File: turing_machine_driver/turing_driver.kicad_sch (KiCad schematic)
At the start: 28 parts, among them J1 Buttons and Switches connector, Q1 55NF06, U1 74LS14, U2 74LS03, U3 74LS04, U4 74LS139, U5 74LS74, U6 NE555P

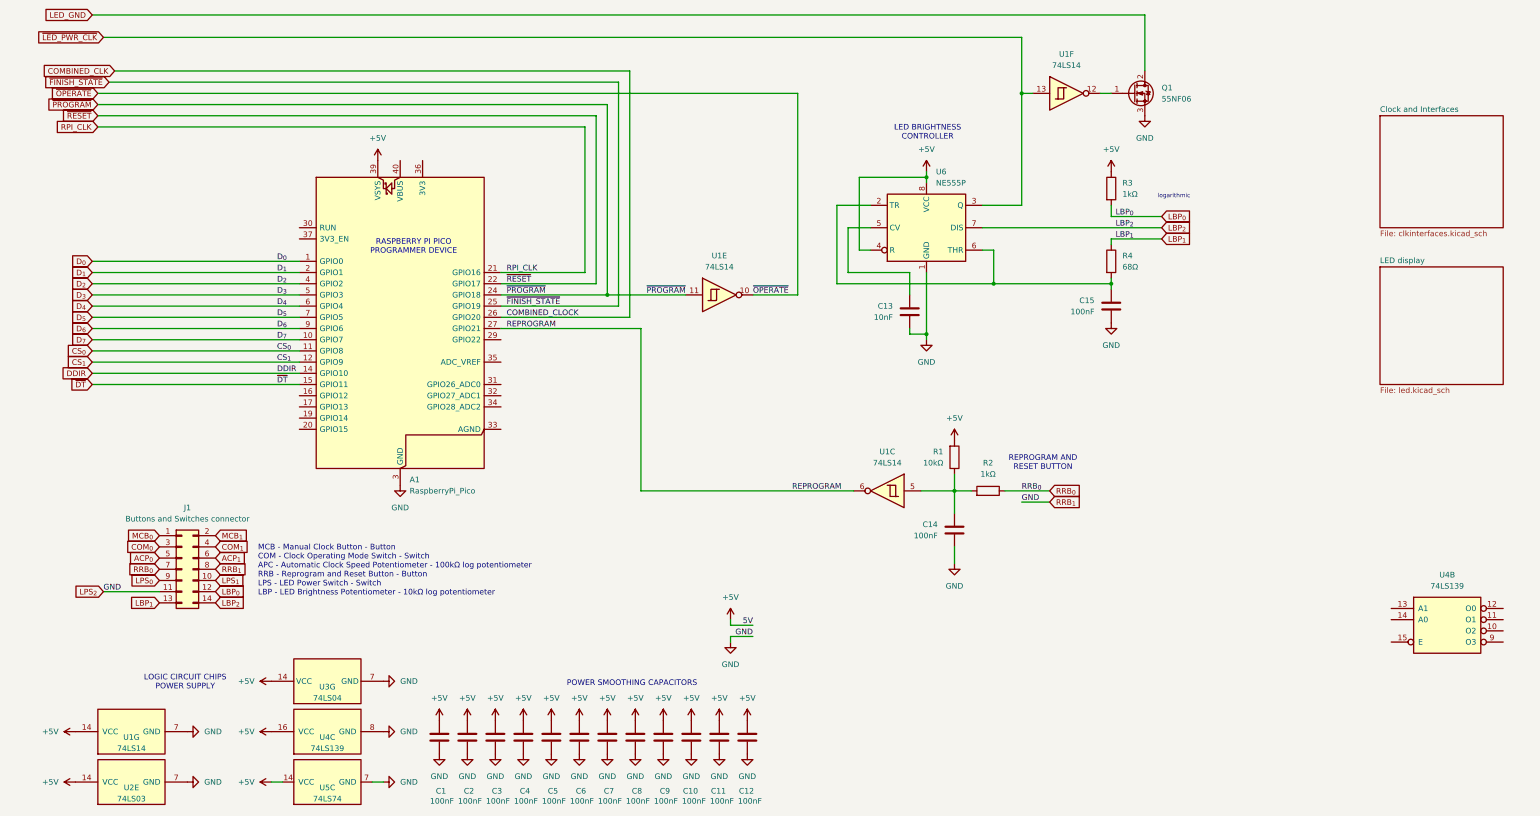
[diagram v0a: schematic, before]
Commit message: added control panel and moved LEDs to it
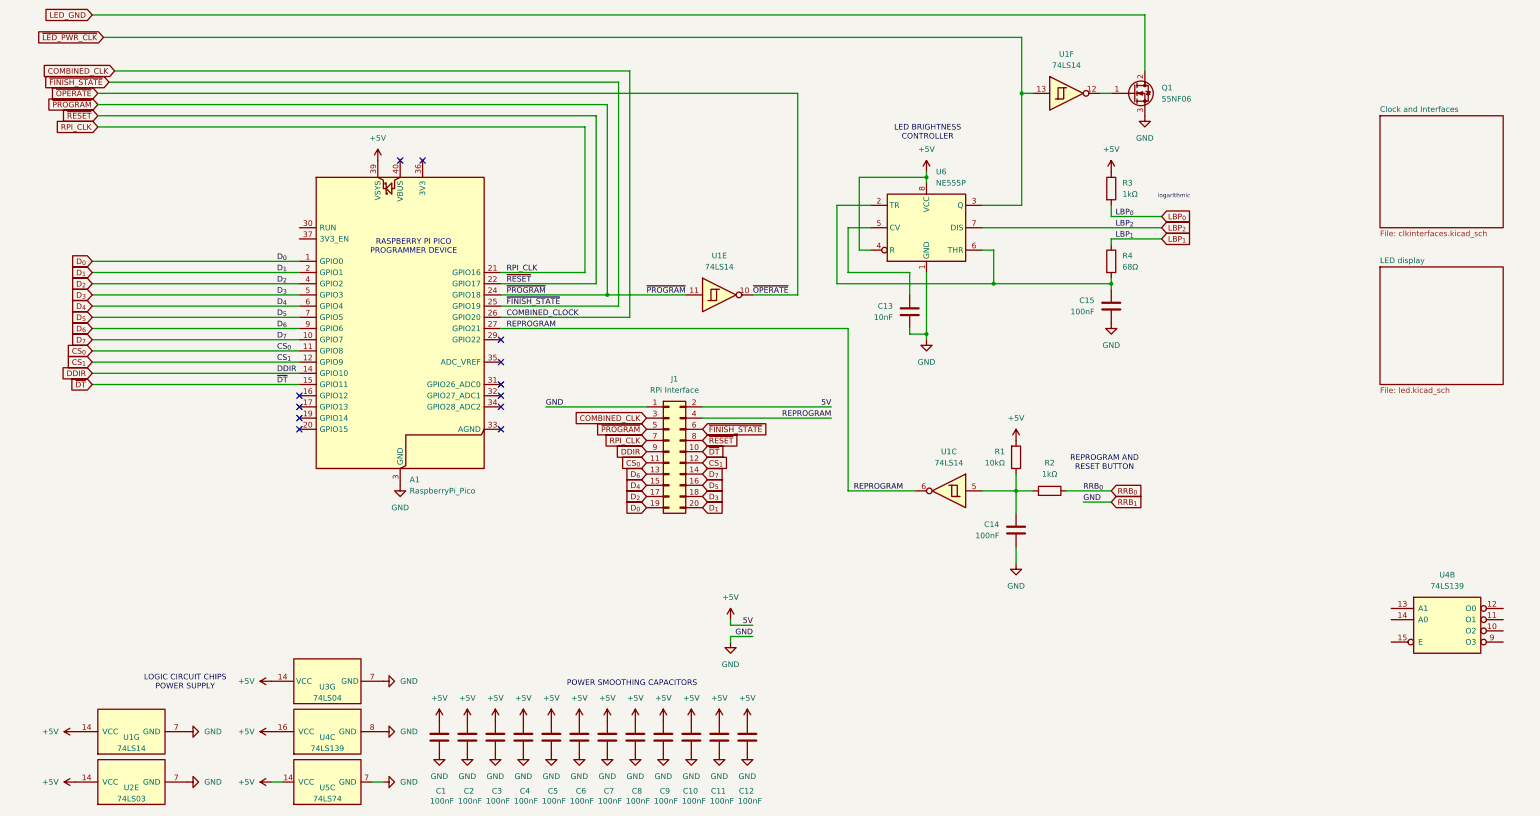
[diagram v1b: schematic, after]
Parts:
- removed J1: Buttons and Switches connector, Connector_IDC:IDC-Header_2x07_P2.54mm_Horizontal, symbol Connector_Generic:Conn_02x07_Odd_Even
- added J1: RPi Interface, Connector_IDC:IDC-Header_2x10_P2.54mm_Vertical, symbol Connector_Generic:Conn_02x10_Odd_Even
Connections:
- net +5V: now also J1.2 (Pin_2)
- net COMBINED_CLK: now also J1.3 (Pin_3)
- net CS_{0}: now also J1.11 (Pin_11)
- net CS_{1}: now also J1.12 (Pin_12)
- net DDIR: now also J1.9 (Pin_9)
- net D_{0}: now also J1.19 (Pin_19)
- net D_{1}: now also J1.20 (Pin_20)
- net D_{2}: now also J1.17 (Pin_17)
- net D_{3}: now also J1.18 (Pin_18)
- net D_{4}: now also J1.15 (Pin_15)
- net D_{5}: now also J1.16 (Pin_16)
- net D_{6}: now also J1.13 (Pin_13)
- net D_{7}: now also J1.14 (Pin_14)
- net GND: now also J1.1 (Pin_1)
- net REPROGRAM: now also J1.4 (Pin_4)
- net RPI_CLK: now also J1.7 (Pin_7)
- net ~{DT}: now also J1.10 (Pin_10)
- net ~{FINISH_STATE}: now also J1.6 (Pin_6)
- net ~{PROGRAM}: now also J1.5 (Pin_5)
- net ~{RESET}: now also J1.8 (Pin_8)
- no-connect marks 0 -> 12
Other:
- note removed: "MCB - Manual Clock Button - Button COM - Clock Operating Mode Switch - Switch APC - Automatic Clock Speed Potentiometer - 100kΩ log potentiometer RRB - Reprogram and Reset Button - Button LPS - LED Power Switch - Switch LBP - LED Brightness Potentiometer - 10kΩ log potentiometer"
- moved on the sheet: C14, R1, R2, U1C

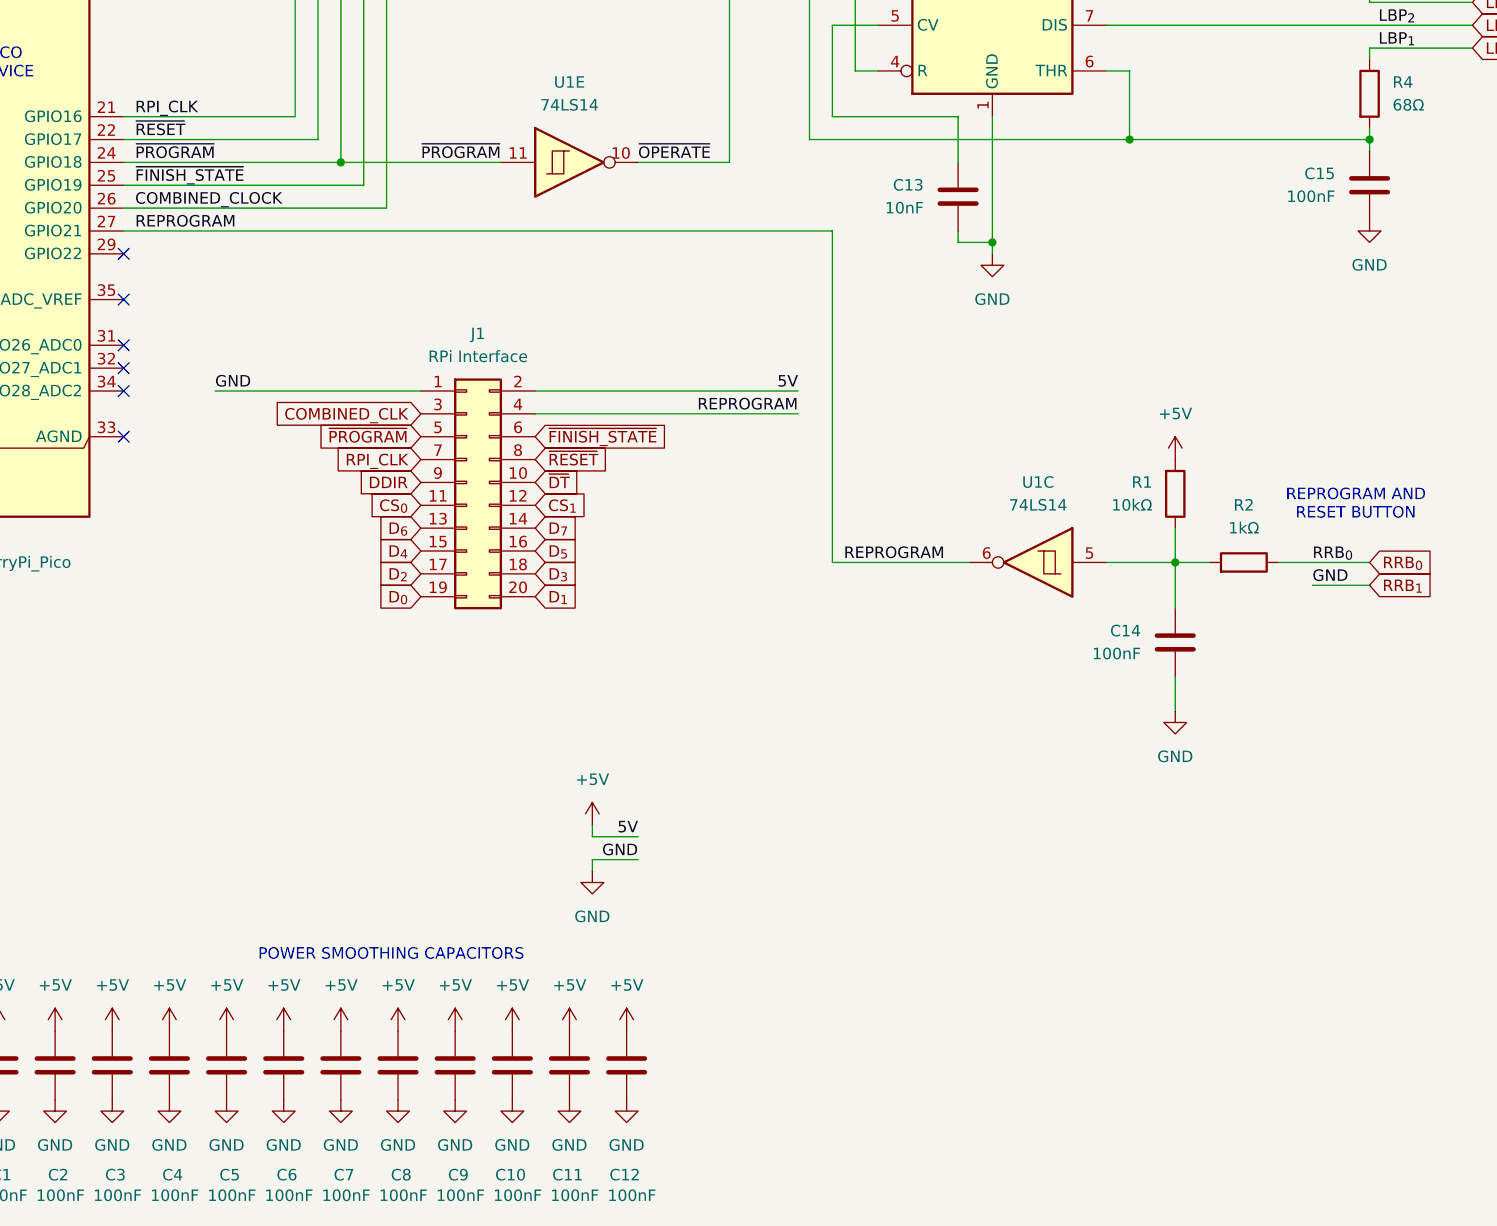
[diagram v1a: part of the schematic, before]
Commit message: finished driver PCB layout
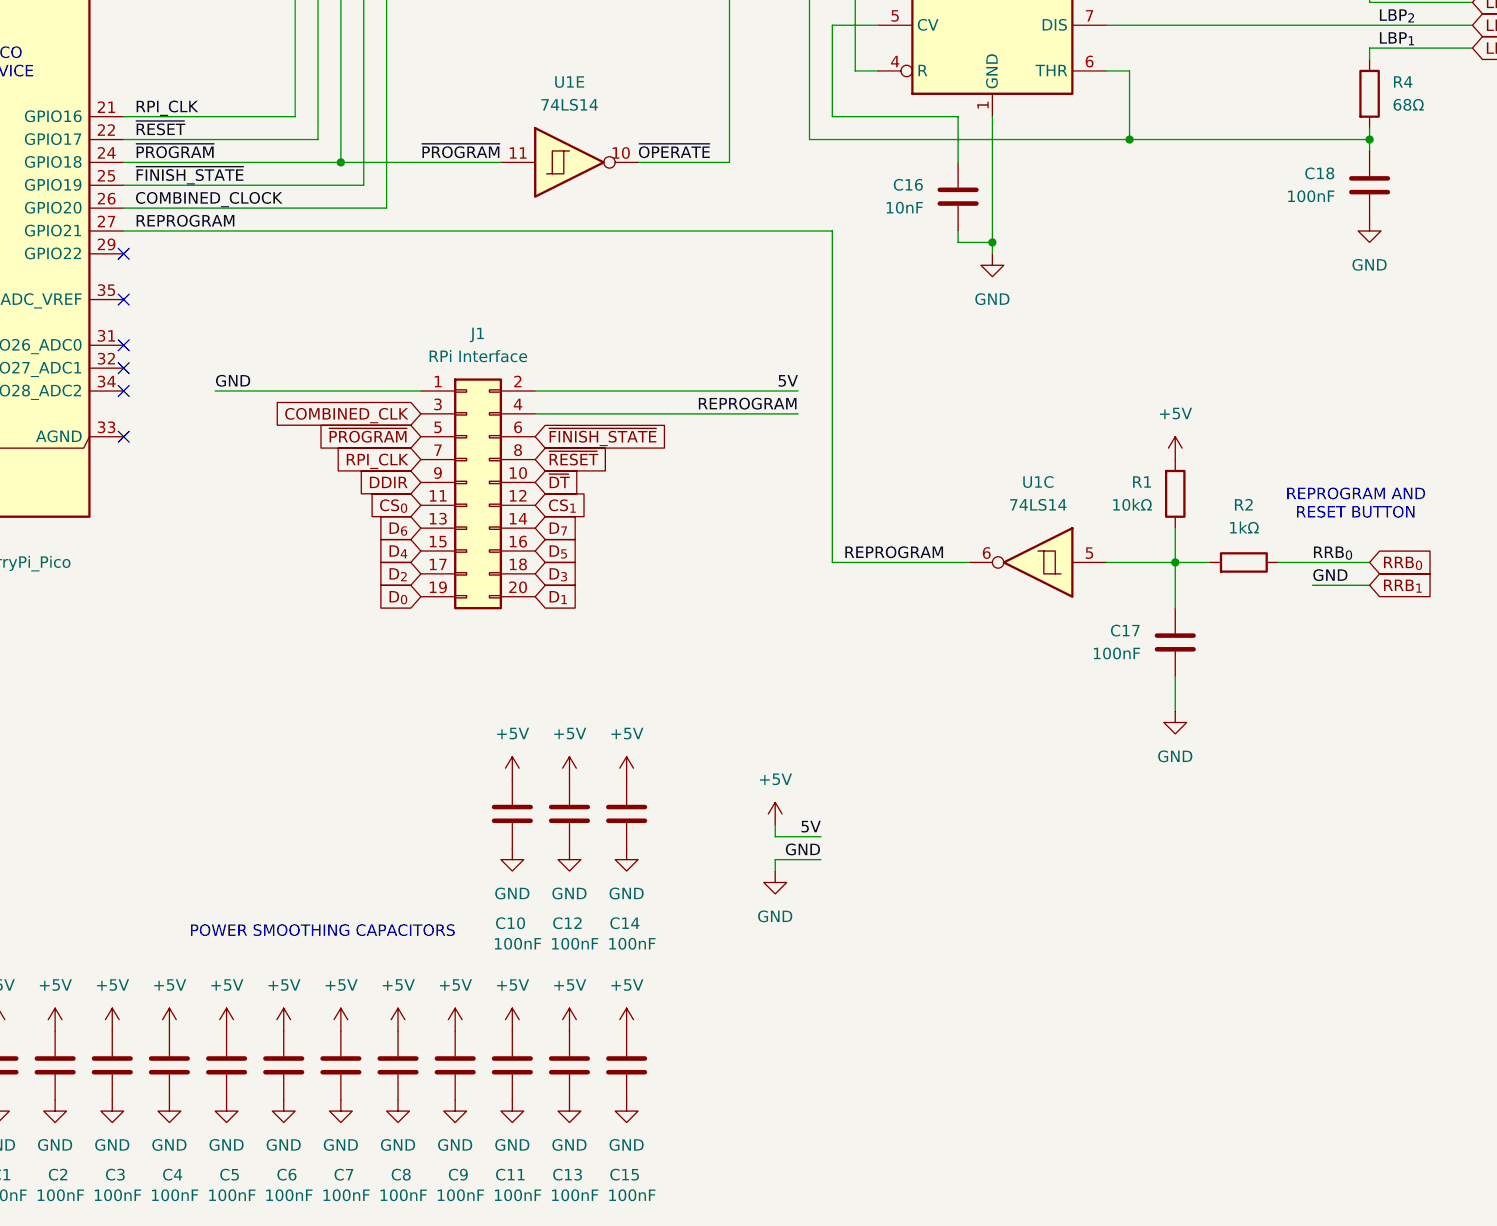
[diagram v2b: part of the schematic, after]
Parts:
- added C10, C12, C14: 100nF, Capacitor_THT:C_Disc_D3.8mm_W2.6mm_P2.50mm, symbol Device:C
- renumbered C10 to C11, C11 to C13, C12 to C15, C13 to C16, C14 to C17, C15 to C18
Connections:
- net +5V: now also C10.1, C12.1, C14.1
- net GND: now also C10.2, C12.2, C14.2

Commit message: added some wiring and fixed few schematic bugs
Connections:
- net +5V: now also U4.13 (A1), U4.14 (A0), U4.15 (E)
- no-connect marks 12 -> 16
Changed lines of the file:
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@@
+	)
+	(no_connect
+		(at 344.17 153.67)
 	)
 	(no_connect
@@
 	)
 	(no_connect
+		(at 344.17 151.13)
+	)
+	(no_connect
 		(at 116.84 95.25)
 	)
 	(no_connect
+		(at 344.17 158.75)
+	)
+	(no_connect
+		(at 344.17 156.21)
+	)
+	(no_connect
 		(at 93.98 49.53)
 	)
@@
 	(wire
 		(pts
+			(xy 318.77 158.75) (xy 313.69 158.75)
+		)
+		(stroke
+			(width 0)
+			(type default)
+		)
+	)
+	(wire
+		(pts
 			(xy 226.06 64.77) (xy 266.7 64.77)
 		)
@@
 	(wire
 		(pts
+			(xy 318.77 151.13) (xy 313.69 151.13)
+		)
+		(stroke
+			(width 0)
+			(type default)
+		)
+	)
+	(wire
+		(pts
 			(xy 24.13 100.33) (xy 71.12 100.33)
 		)
@@
 		(pts
 			(xy 252.73 34.29) (xy 255.27 34.29)
+		)
+		(stroke
+			(width 0)
+			(type default)
+		)
+	)
+	(wire
+		(pts
+			(xy 318.77 153.67) (xy 313.69 153.67)
 		)
 		(stroke
@@
 		)
 	)
+	(label "5V"
+		(at 313.69 151.13 0)
+		(effects
+			(font
+				(size 1.27 1.27)
+			)
+			(justify left bottom)
+		)
+	)
 	(label "~{OPERATE}"
 		(at 173.99 80.01 0)
@@
 		)
 	)
+	(label "5V"
+		(at 313.69 158.75 0)
+		(effects
+			(font
+				(size 1.27 1.27)
+			)
+			(justify left bottom)
+		)
+	)
 	(label "D_{5}"
 		(at 66.04 85.09 0)
@@
 		(effects
 			(font
+				(size 1.27 1.27)
+			)
+			(justify left bottom)
+		)
+	)
+	(label "5V"
+		(at 313.69 153.67 0)
+		(effects
+			(font
